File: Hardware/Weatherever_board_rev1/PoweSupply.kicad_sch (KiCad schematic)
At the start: 17 parts

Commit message: Finished HW schematic and minor project cleanup
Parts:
- gave numbers to parts that had none: 16
- renumbered C2 to C201
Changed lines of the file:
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@@
   (symbol (lib_id "Device:C_Polarized") (at 180.975 62.865 0) (unit 1)
     (in_bom yes) (on_board yes)
-    (property "Reference" "C?" (id 0) (at 181.61 60.325 0)
+    (property "Reference" "C202" (id 0) (at 181.61 60.325 0)
       (effects (font (size 1.27 1.27)) (justify left))
     )
@@
   (symbol (lib_id "Device:C_Polarized") (at 188.595 114.935 0) (unit 1)
     (in_bom yes) (on_board yes) (fields_autoplaced)
-    (property "Reference" "C?" (id 0) (at 191.77 112.7759 0)
+    (property "Reference" "C206" (id 0) (at 191.77 112.7759 0)
       (effects (font (size 1.27 1.27)) (justify left))
     )
@@
   (symbol (lib_id "Device:C_Polarized") (at 137.16 112.395 0) (unit 1)
     (in_bom yes) (on_board yes) (fields_autoplaced)
-    (property "Reference" "C?" (id 0) (at 140.97 110.2359 0)
+    (property "Reference" "C205" (id 0) (at 140.97 110.2359 0)
       (effects (font (size 1.27 1.27)) (justify left))
     )
@@
   (symbol (lib_id "Device:D_Bridge_+-AA") (at 163.83 62.23 0) (unit 1)
     (in_bom yes) (on_board yes)
-    (property "Reference" "D?" (id 0) (at 170.18 57.785 0))
+    (property "Reference" "D202" (id 0) (at 170.18 57.785 0))
     (property "Value" "MB05F" (id 1) (at 170.18 67.31 0))
     (property "Footprint" "" (id 2) (at 163.83 62.23 0)
@@
   (symbol (lib_id "CustomSymbols:L78M09CDT") (at 205.105 104.14 0) (unit 1)
     (in_bom yes) (on_board yes) (fields_autoplaced)
-    (property "Reference" "U?" (id 0) (at 206.375 100.965 0))
+    (property "Reference" "U201" (id 0) (at 206.375 100.965 0))
     (property "Value" "L78M09CDT" (id 1) (at 206.375 103.505 0))
     (property "Footprint" "Package_TO_SOT_SMD:TO-252-2" (id 2) (at 205.105 104.14 0)
@@
   (symbol (lib_id "Device:C_Polarized") (at 180.975 39.37 0) (unit 1)
     (in_bom yes) (on_board yes)
-    (property "Reference" "C2" (id 0) (at 181.61 36.83 0)
+    (property "Reference" "C201" (id 0) (at 181.61 36.83 0)
       (effects (font (size 1.27 1.27)) (justify left))
     )
@@
   (symbol (lib_id "Device:L") (at 116.205 106.68 90) (unit 1)
     (in_bom yes) (on_board yes) (fields_autoplaced)
-    (property "Reference" "L?" (id 0) (at 116.205 100.965 90))
+    (property "Reference" "L201" (id 0) (at 116.205 100.965 90))
     (property "Value" "2u2" (id 1) (at 116.205 103.505 90))
     (property "Footprint" "" (id 2) (at 116.205 106.68 0)
@@
   (symbol (lib_id "power:+3V3") (at 141.605 105.41 0) (unit 1)
     (in_bom yes) (on_board yes) (fields_autoplaced)
-    (property "Reference" "#PWR?" (id 0) (at 141.605 109.22 0)
+    (property "Reference" "#PWR0203" (id 0) (at 141.605 109.22 0)
       (effects (font (size 1.27 1.27)) hide)
     )
@@
   (symbol (lib_id "Connector:Screw_Terminal_01x02") (at 111.125 52.07 180) (unit 1)
     (in_bom yes) (on_board yes)
-    (property "Reference" "J?" (id 0) (at 111.125 44.5602 0))
+    (property "Reference" "J201" (id 0) (at 111.125 44.5602 0))
     (property "Value" "Mains (230V, 50Hz)" (id 1) (at 111.76 46.99 0))
     (property "Footprint" "" (id 2) (at 111.125 52.07 0)
@@
   (symbol (lib_id "Device:C_Polarized") (at 76.2 109.855 0) (mirror y) (unit 1)
     (in_bom yes) (on_board yes)
-    (property "Reference" "C?" (id 0) (at 71.755 107.315 0)
+    (property "Reference" "C204" (id 0) (at 71.755 107.315 0)
       (effects (font (size 1.27 1.27)) (justify right))
     )
@@
   (symbol (lib_id "power:GNDD") (at 121.92 120.65 0) (unit 1)
     (in_bom yes) (on_board yes) (fields_autoplaced)
-    (property "Reference" "#PWR?" (id 0) (at 121.92 127 0)
+    (property "Reference" "#PWR0208" (id 0) (at 121.92 127 0)
       (effects (font (size 1.27 1.27)) hide)
     )
@@
   (symbol (lib_id "Device:D_Bridge_+-AA") (at 163.83 38.735 0) (unit 1)
     (in_bom yes) (on_board yes)
-    (property "Reference" "D?" (id 0) (at 170.18 34.29 0))
+    (property "Reference" "D201" (id 0) (at 170.18 34.29 0))
     (property "Value" "MB05F" (id 1) (at 170.18 43.815 0))
     (property "Footprint" "" (id 2) (at 163.83 38.735 0)
@@
   (symbol (lib_id "Device:C") (at 222.25 114.935 0) (unit 1)
     (in_bom yes) (on_board yes) (fields_autoplaced)
-    (property "Reference" "C?" (id 0) (at 225.425 113.6649 0)
+    (property "Reference" "C207" (id 0) (at 225.425 113.6649 0)
       (effects (font (size 1.27 1.27)) (justify left))
     )
@@
   (symbol (lib_id "power:+9V") (at 231.775 107.315 0) (unit 1)
     (in_bom yes) (on_board yes) (fields_autoplaced)
-    (property "Reference" "#PWR?" (id 0) (at 231.775 111.125 0)
+    (property "Reference" "#PWR0204" (id 0) (at 231.775 111.125 0)
       (effects (font (size 1.27 1.27)) hide)
     )
@@
   (symbol (lib_id "Device:R_Small") (at 121.92 110.49 0) (unit 1)
     (in_bom yes) (on_board yes) (fields_autoplaced)
-    (property "Reference" "R?" (id 0) (at 124.46 109.2199 0)
+    (property "Reference" "R201" (id 0) (at 124.46 109.2199 0)
       (effects (font (size 1.27 1.27)) (justify left))
     )
@@
   (symbol (lib_id "Device:Transformer_1P_2S") (at 135.89 50.8 0) (unit 1)
     (in_bom yes) (on_board yes)
-    (property "Reference" "T?" (id 0) (at 135.89 37.0671 0))
+    (property "Reference" "T201" (id 0) (at 135.89 37.0671 0))
     (property "Value" "TEZ2.5/D230/10.5-10.5V" (id 1) (at 135.89 63.5 0))
     (property "Footprint" "" (id 2) (at 135.89 50.8 0)
@@
   (symbol (lib_id "power:GNDD") (at 107.95 120.65 0) (unit 1)
     (in_bom yes) (on_board yes) (fields_autoplaced)
-    (property "Reference" "#PWR?" (id 0) (at 107.95 127 0)
+    (property "Reference" "#PWR0207" (id 0) (at 107.95 127 0)
       (effects (font (size 1.27 1.27)) hide)
     )
@@
   (symbol (lib_id "Device:D_Schottky") (at 107.95 114.935 270) (unit 1)
     (in_bom yes) (on_board yes) (fields_autoplaced)
-    (property "Reference" "D?" (id 0) (at 110.49 113.3474 90)
+    (property "Reference" "D203" (id 0) (at 110.49 113.3474 90)
       (effects (font (size 1.27 1.27)) (justify left))
     )
@@
   (symbol (lib_id "Device:R_Small") (at 121.92 118.11 0) (unit 1)
     (in_bom yes) (on_board yes) (fields_autoplaced)
-    (property "Reference" "R?" (id 0) (at 124.46 116.8399 0)
+    (property "Reference" "R202" (id 0) (at 124.46 116.8399 0)
       (effects (font (size 1.27 1.27)) (justify left))
     )
@@
   (symbol (lib_id "power:GNDD") (at 76.2 120.65 0) (unit 1)
     (in_bom yes) (on_board yes) (fields_autoplaced)
-    (property "Reference" "#PWR?" (id 0) (at 76.2 127 0)
+    (property "Reference" "#PWR0205" (id 0) (at 76.2 127 0)
       (effects (font (size 1.27 1.27)) hide)
     )
@@
   (symbol (lib_id "power:GNDD") (at 93.98 120.65 0) (unit 1)
     (in_bom yes) (on_board yes) (fields_autoplaced)
-    (property "Reference" "#PWR?" (id 0) (at 93.98 127 0)
+    (property "Reference" "#PWR0206" (id 0) (at 93.98 127 0)
       (effects (font (size 1.27 1.27)) hide)
     )
@@
   (symbol (lib_id "power:GNDD") (at 137.16 120.65 0) (unit 1)
     (in_bom yes) (on_board yes) (fields_autoplaced)
-    (property "Reference" "#PWR?" (id 0) (at 137.16 127 0)
+    (property "Reference" "#PWR0209" (id 0) (at 137.16 127 0)
       (effects (font (size 1.27 1.27)) hide)
     )
@@
   (symbol (lib_id "power:GNDD") (at 185.42 71.12 0) (unit 1)
     (in_bom yes) (on_board yes) (fields_autoplaced)
-    (property "Reference" "#PWR?" (id 0) (at 185.42 77.47 0)
+    (property "Reference" "#PWR0202" (id 0) (at 185.42 77.47 0)
       (effects (font (size 1.27 1.27)) hide)
     )
@@
   (symbol (lib_id "power:GND1") (at 185.42 47.625 0) (unit 1)
     (in_bom yes) (on_board yes)
-    (property "Reference" "#PWR?" (id 0) (at 185.42 53.975 0)
+    (property "Reference" "#PWR0201" (id 0) (at 185.42 53.975 0)
       (effects (font (size 1.27 1.27)) hide)
     )
@@
   (symbol (lib_id "Device:C_Small") (at 107.315 100.965 90) (unit 1)
     (in_bom yes) (on_board yes)
-    (property "Reference" "C?" (id 0) (at 107.315 95.885 90))
+    (property "Reference" "C203" (id 0) (at 107.315 95.885 90))
     (property "Value" "10n" (id 1) (at 107.315 97.79 90))
     (property "Footprint" "" (id 2) (at 107.315 100.965 0)
@@
   (symbol (lib_id "power:GND1") (at 206.375 124.46 0) (unit 1)
     (in_bom yes) (on_board yes)
-    (property "Reference" "#PWR?" (id 0) (at 206.375 130.81 0)
+    (property "Reference" "#PWR0210" (id 0) (at 206.375 130.81 0)
       (effects (font (size 1.27 1.27)) hide)
     )
@@
   (symbol (lib_id "Regulator_Switching:AOZ1280CI") (at 93.98 106.68 0) (unit 1)
     (in_bom yes) (on_board yes) (fields_autoplaced)
-    (property "Reference" "U?" (id 0) (at 93.98 97.9002 0))
+    (property "Reference" "U202" (id 0) (at 93.98 97.9002 0))
     (property "Value" "AOZ1280CI" (id 1) (at 93.98 100.4371 0))
     (property "Footprint" "Package_TO_SOT_SMD:SOT-23-6" (id 2) (at 111.76 113.03 0)

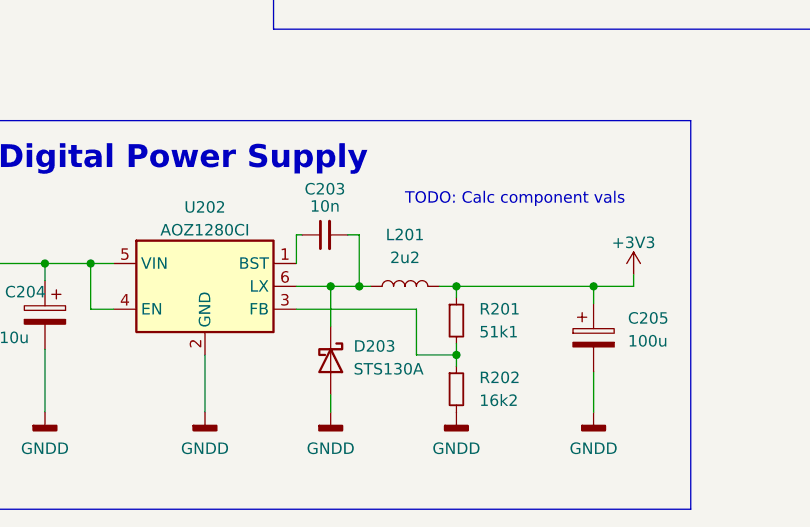
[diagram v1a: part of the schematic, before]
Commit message: New hw element and CommHandler tests
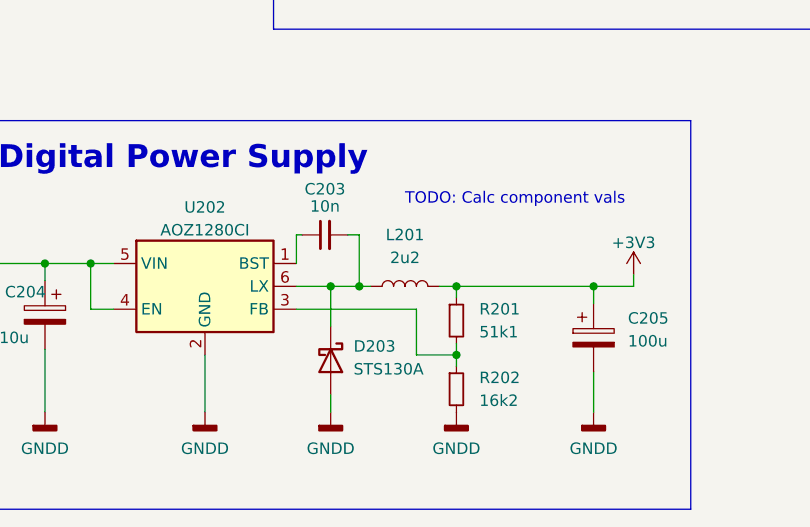
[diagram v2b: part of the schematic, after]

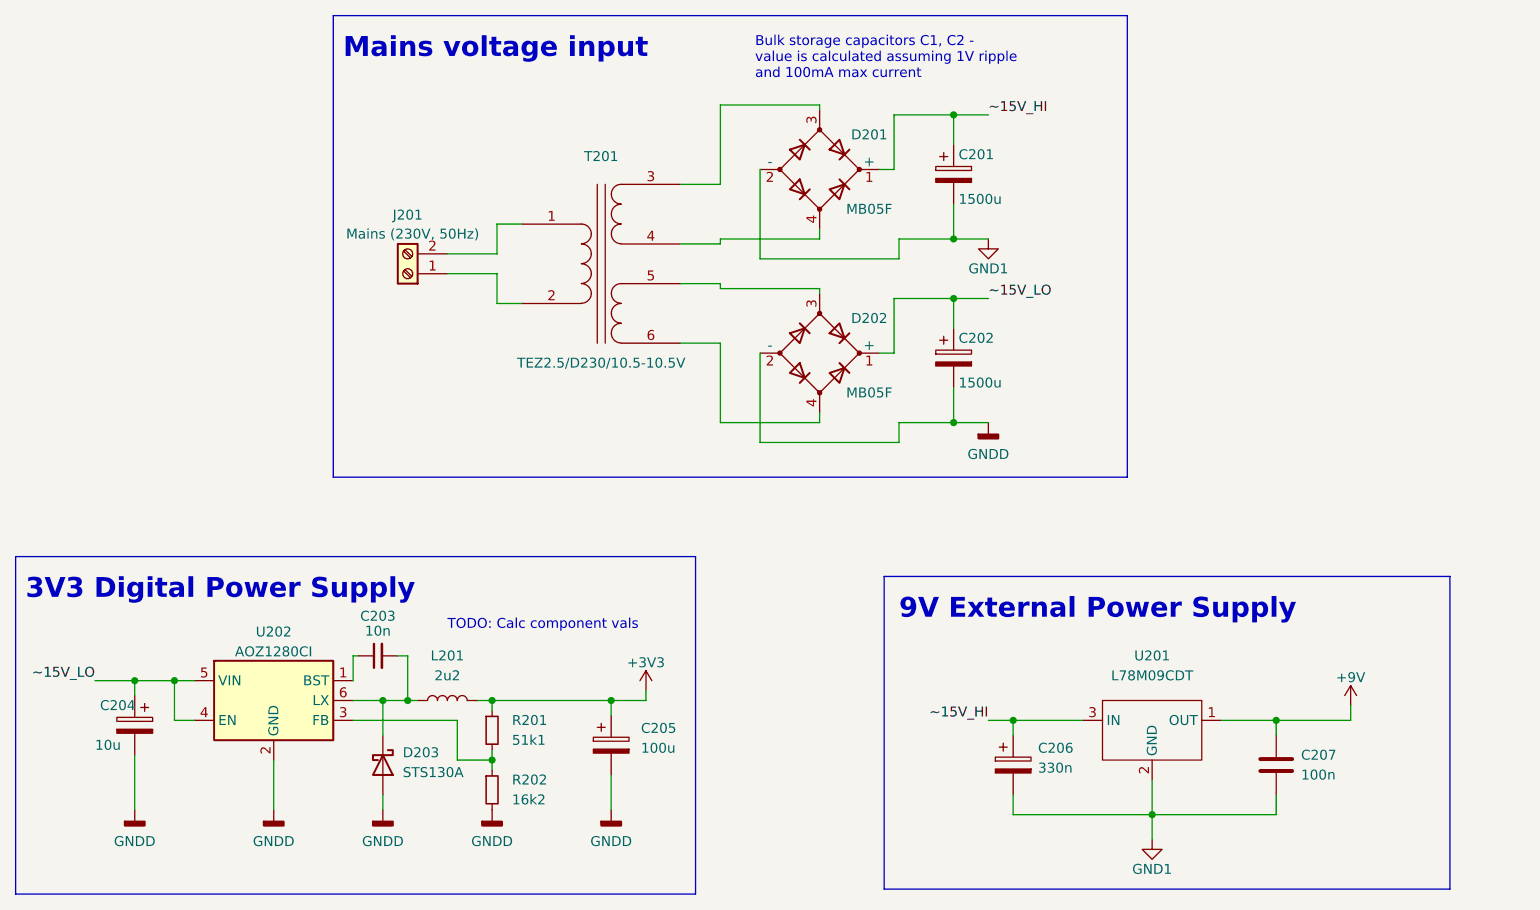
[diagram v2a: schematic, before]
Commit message: Funished schematics and GPIO drv interface
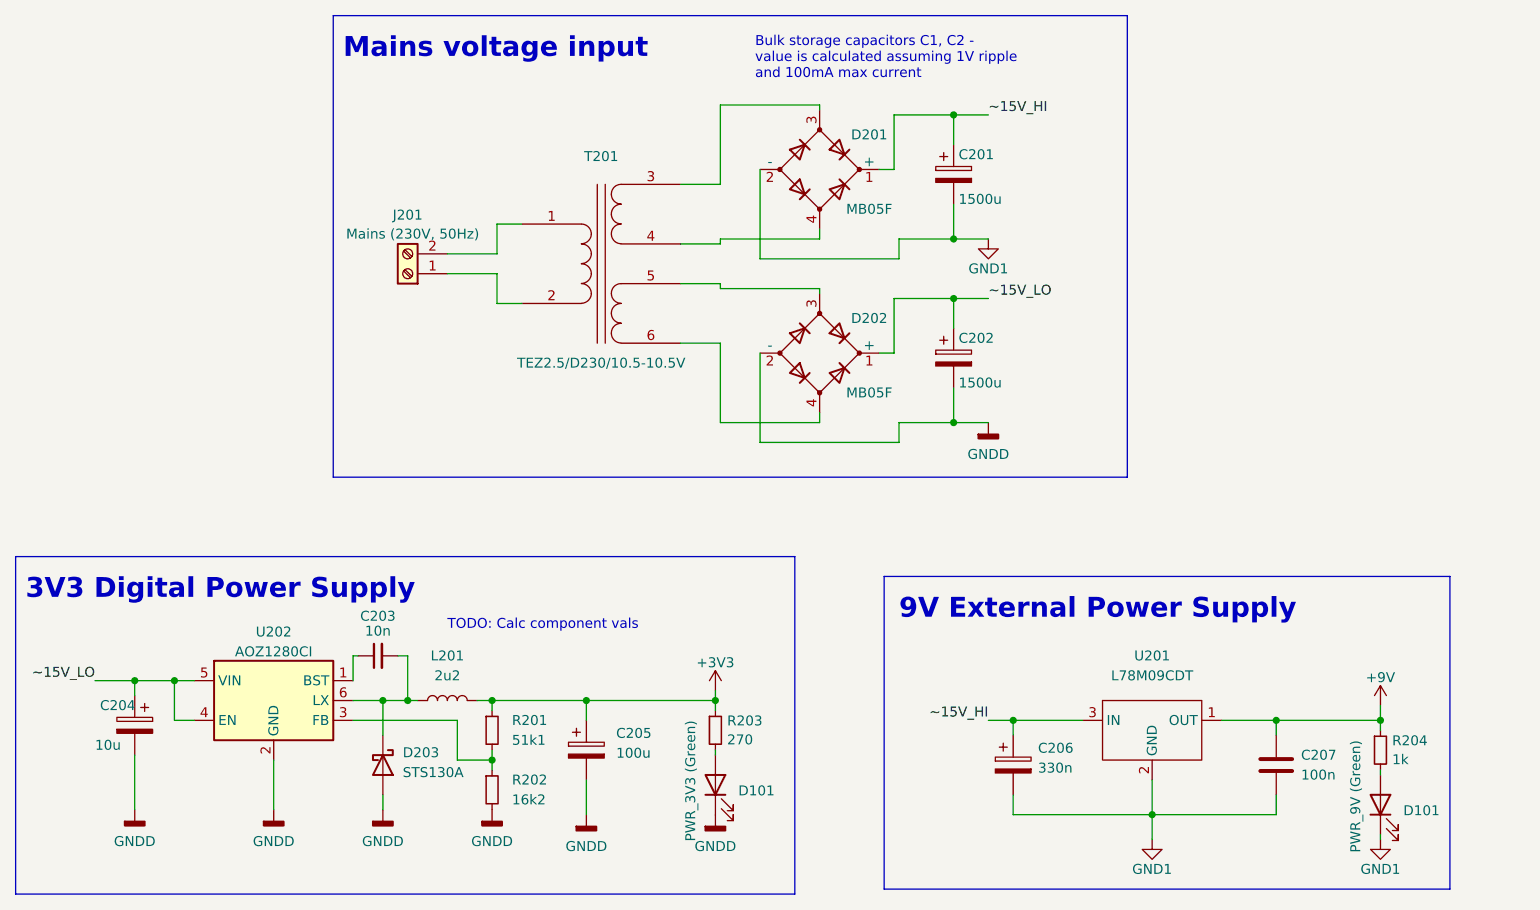
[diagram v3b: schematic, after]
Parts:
- added D101: PWR_9V (Green), LED_SMD:LED_0805_2012Metric_Pad1.15x1.40mm_HandSolder, symbol Device:LED
- added D101: PWR_3V3 (Green), LED_SMD:LED_0805_2012Metric_Pad1.15x1.40mm_HandSolder, symbol Device:LED
- added R203: 270, symbol Device:R_Small
- added R204: 1k, symbol Device:R_Small
- T201: footprint (none) -> Transformer_THT:Transformer_Breve_TEZ-28x33
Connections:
- net +3V3: now also R203.1
- net +9V: now also R204.1
- net GND1: now also D101.1 (K)
- net GNDD: now also D101.1 (K)
- new net: D101.2 (A), R203.2
- new net: D101.2 (A), R204.2
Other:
- moved on the sheet: C205

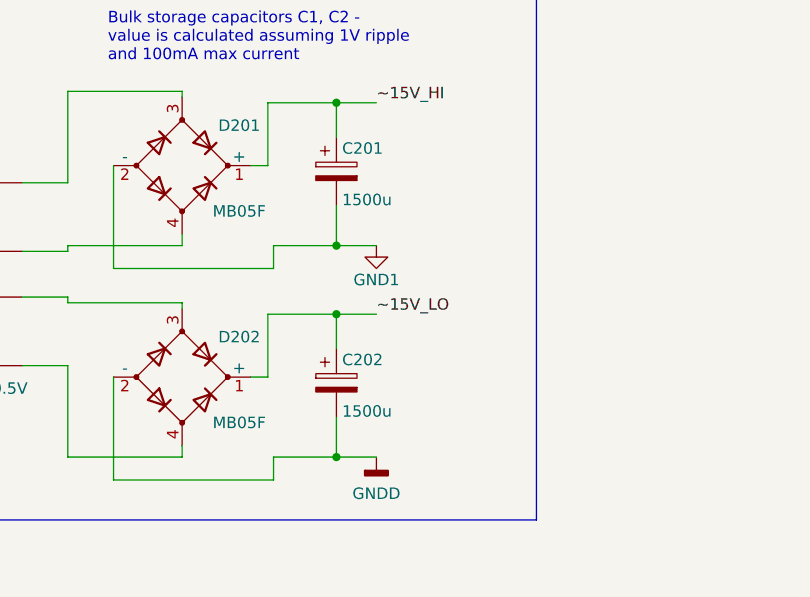
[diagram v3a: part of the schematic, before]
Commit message: Some components footprint updates
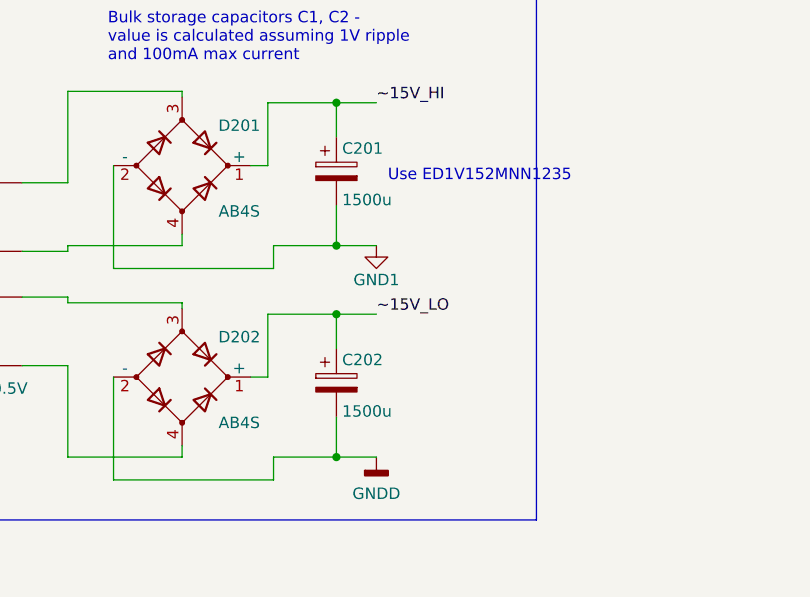
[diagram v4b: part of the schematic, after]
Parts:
- C201, C202: footprint (none) -> Capacitor_THT:CP_Radial_D12.5mm_P5.00mm
- C205: footprint (none) -> Capacitor_SMD:CP_Elec_6.3x5.4
- D201, D202: value MB05F -> AB4S; footprint (none) -> Diode_SMD:Diode_Bridge_Diotec_ABS
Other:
- note added: "Use ED1V152MNN1235"
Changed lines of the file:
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@@
+    (effects (font (size 1.27 1.27)) (justify left bottom))
+  )
+  (text "Use ED1V152MNN1235" (at 186.69 40.64 0)
     (effects (font (size 1.27 1.27)) (justify left bottom))
   )
@@
       (effects (font (size 1.27 1.27)) (justify left))
     )
-    (property "Footprint" "" (at 181.9402 66.675 0)
+    (property "Footprint" "Capacitor_THT:CP_Radial_D12.5mm_P5.00mm" (at 181.9402 66.675 0)
       (effects (font (size 1.27 1.27)) hide)
     )
@@
       (effects (font (size 1.27 1.27)) (justify left))
     )
-    (property "Footprint" "" (at 134.9502 116.84 0)
+    (property "Footprint" "Capacitor_SMD:CP_Elec_6.3x5.4" (at 134.9502 116.84 0)
       (effects (font (size 1.27 1.27)) hide)
     )
@@
       (effects (font (size 1.27 1.27)))
     )
-    (property "Value" "MB05F" (at 170.18 67.31 0)
-      (effects (font (size 1.27 1.27)))
-    )
-    (property "Footprint" "" (at 163.83 62.23 0)
+    (property "Value" "AB4S" (at 170.18 67.31 0)
+      (effects (font (size 1.27 1.27)))
+    )
+    (property "Footprint" "Diode_SMD:Diode_Bridge_Diotec_ABS" (at 163.83 62.23 0)
       (effects (font (size 1.27 1.27)) hide)
     )
@@
       (effects (font (size 1.27 1.27)) (justify left))
     )
-    (property "Footprint" "" (at 181.9402 43.18 0)
+    (property "Footprint" "Capacitor_THT:CP_Radial_D12.5mm_P5.00mm" (at 181.9402 43.18 0)
       (effects (font (size 1.27 1.27)) hide)
     )
@@
       (effects (font (size 1.27 1.27)))
     )
-    (property "Value" "MB05F" (at 170.18 43.815 0)
-      (effects (font (size 1.27 1.27)))
-    )
-    (property "Footprint" "" (at 163.83 38.735 0)
-      (effects (font (size 1.27 1.27)) hide)
-    )
+    (property "Value" "AB4S" (at 170.18 43.815 0)
+      (effects (font (size 1.27 1.27)))
+    )
+    (property "Footprint" "Diode_SMD:Diode_Bridge_Diotec_ABS" (at 163.83 38.735 0)
+      (effects (font (size 1.27 1.27)) hide)
+    )

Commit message: Layout impl start
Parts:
- added R205: 10k, Resistor_SMD:R_0805_2012Metric_Pad1.20x1.40mm_HandSolder, symbol Device:R_Small
- C203, C204, C206, C207: footprint (none) -> Capacitor_SMD:C_0805_2012Metric_Pad1.18x1.45mm_HandSolder
- D101: value PWR_9V (Green) -> PWR_9V
- D101: value PWR_3V3 (Green) -> PWR_3V3
- D203: footprint (none) -> Diode_SMD:D_SMA-SMB_Universal_Handsoldering
- J201: footprint (none) -> TerminalBlock_Phoenix:TerminalBlock_Phoenix_MKDS-1,5-2-5.08_1x02_P5.08mm_Horizontal
- L201: footprint (none) -> Inductor_SMD:L_0805_2012Metric_Pad1.15x1.40mm_HandSolder
- R201, R202, R203, R204: footprint (none) -> Resistor_SMD:R_0805_2012Metric_Pad1.20x1.40mm_HandSolder
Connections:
- net ~15V_LO: now also R205.1; no longer U202.4 (EN)
- net at T201.5 (AB): now also J201.1 (Pin_1); no longer D202.3
- net 10V5AC_HI1: now reaches T201.6 (SA)
- net 10V5AC_HI1: now also D201.4; no longer D202.4
- net 10V5AC_HI2: now reaches D201.3
- net 10V5AC_HI2: now also T201.7 (SB); no longer T201.3 (SA)
- new net: R205.2, U202.4 (EN)
- new net 10V5AC_LO1: D202.4, T201.9 (SC)
- new net 10V5AC_LO2: D202.3, T201.10 (SD)
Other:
- moved on the sheet: C203, C204, C205, C206, C207, D101, D203, L201, R201, R202, R203, R204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
